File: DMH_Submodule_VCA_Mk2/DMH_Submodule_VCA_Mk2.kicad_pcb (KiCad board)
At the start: 2 copper layers, 41 x 27 mm, 20 parts, among them J1 Conn_01x02, J2 Conn_01x04, Q1 BC548, Q2 BC548, U1 TL072

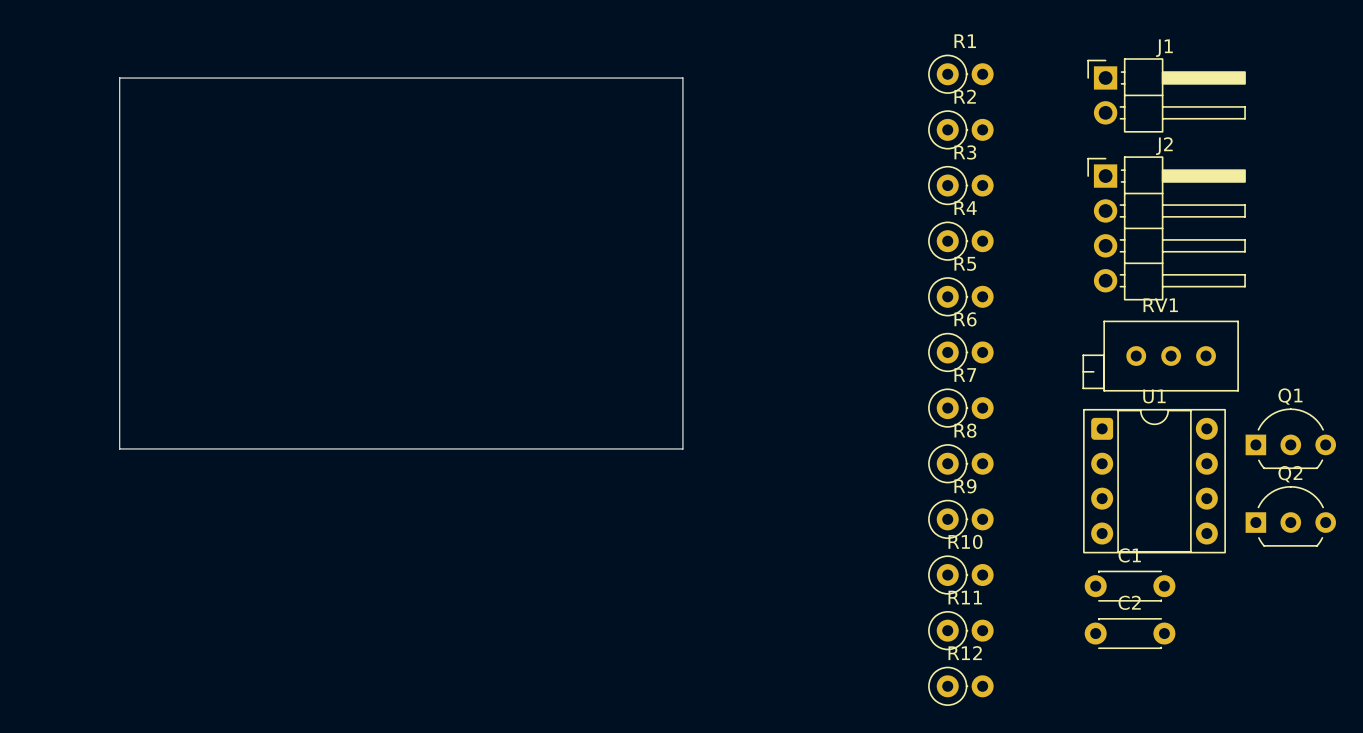
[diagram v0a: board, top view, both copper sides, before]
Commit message: Routed VCA submodule Mk2 PCB
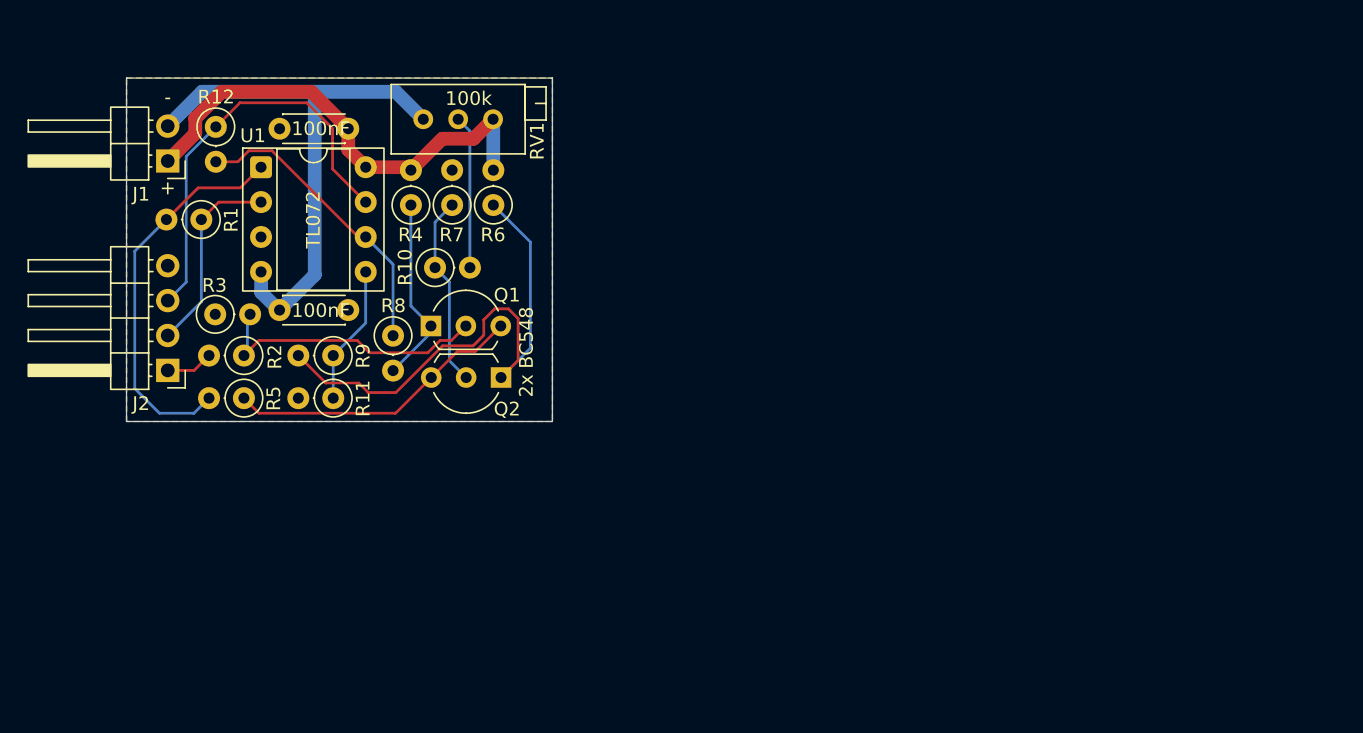
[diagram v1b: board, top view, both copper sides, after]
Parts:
- moved J2 69.7 mm to (57.5, 70.8), turned to 180 degrees
- moved J1 68.5 mm to (57.5, 55.5), turned to 180 degrees
- moved R12 67.1 mm to (61.0, 53.1), turned to -90 degrees
- moved U1 64.1 mm to (64.3, 56.0)
- moved C1 63.8 mm to (70.6, 53.2), turned to 180 degrees
- moved Q1 60.7 mm to (76.7, 67.5)
- moved RV1 59.5 mm to (76.1, 52.5), turned to 180 degrees
- moved C2 59.3 mm to (70.6, 66.4), turned to 180 degrees
- moved Q2 55.9 mm to (81.8, 71.3), turned to 180 degrees
- moved R1 55.3 mm to (59.9, 59.8), turned to 180 degrees
- moved R3 54.1 mm to (61.0, 66.7)
- moved R2 53.8 mm to (63.0, 69.7), turned to 180 degrees
- moved R5 51.8 mm to (63.0, 72.8), turned to 180 degrees
- moved R11 47.8 mm to (69.5, 72.8), turned to 180 degrees
- moved R9 46.3 mm to (69.5, 69.7), turned to 180 degrees
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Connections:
- R10 pad 1: Net-(R10-Pad1) -> Net-(Q2-B)
- R10 pad 2: Net-(Q2-B) -> Net-(R10-Pad2)
- R5 pad 1: Net-(R1-Pad2) -> Net-(Q1-E)
- R5 pad 2: Net-(Q1-E) -> Net-(R1-Pad2)
- R7 pad 1: GND -> Net-(Q2-B)
- R7 pad 2: Net-(Q2-B) -> GND
- RV1 pad 2: Net-(R10-Pad1) -> Net-(R10-Pad2)
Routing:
- net -12V: track 0.00 -> 40.8 mm
- net Net-(Q2-C): track 0.00 -> 40.0 mm
- net +12V: track 0.00 -> 34.9 mm
- net /Signal_Out: track 0.00 -> 30.4 mm
- net Net-(R1-Pad2): track 0.00 -> 28.3 mm
- net Net-(U1B--): track 0.00 -> 21.8 mm
- net Net-(Q1-E): track 0.00 -> 21.8 mm
- net Net-(Q1-B): track 0.00 -> 21.0 mm
- net /CV_Mix_In: track 0.00 -> 14.3 mm
- net Net-(Q2-B): track 0.00 -> 14.0 mm
- net Net-(Q1-C): track 0.00 -> 13.8 mm
- net Net-(R10-Pad2): track 0.00 -> 11.2 mm
- net Net-(U1B-+): track 0.00 -> 10.2 mm
- net /Signal_In: track 0.00 -> 3.45 mm
- added copper zone on B.Cu, net GND
- added copper zone on F.Cu, net GND
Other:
- board size 41 x 27 mm -> 31 x 25 mm
- board text added: "+"
- board text added: "-"
- board text added: "2x"
- board text added: "Mk2.0 July 2026"
- board text removed: "Mk1.0 June 2026"

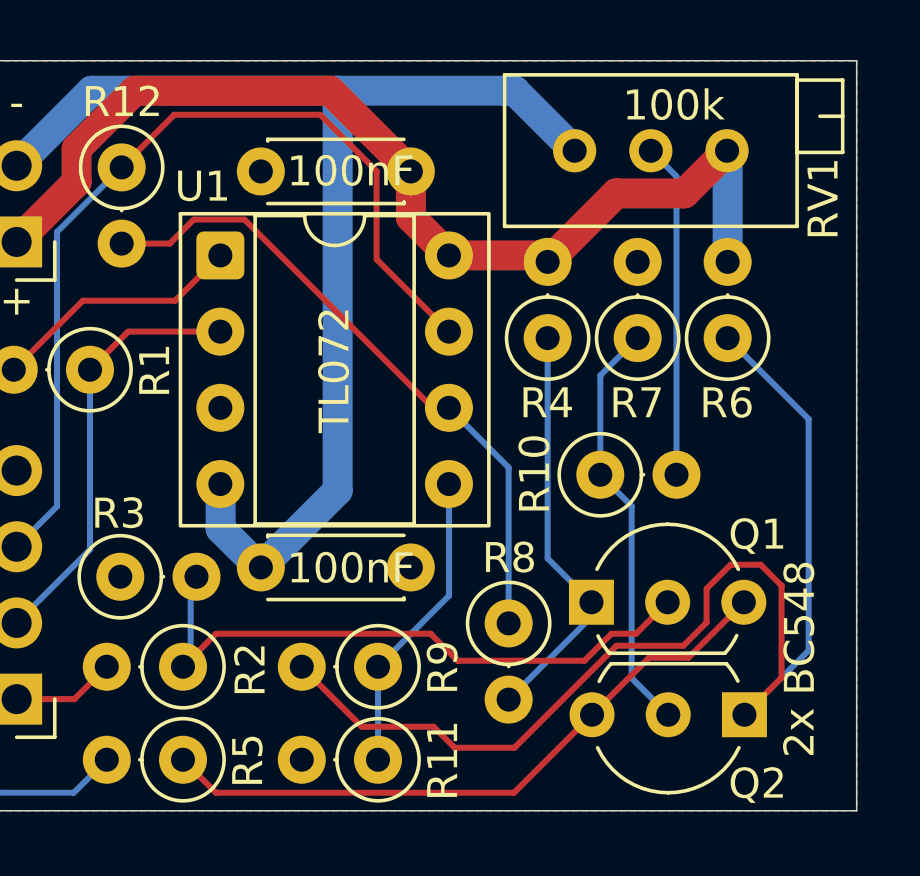
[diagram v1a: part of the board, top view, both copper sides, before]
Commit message: Redesigned PCB
Included solder bridge jumpers to selected between inverting and non-inverting mode. Added C5 for high freq stabilization.
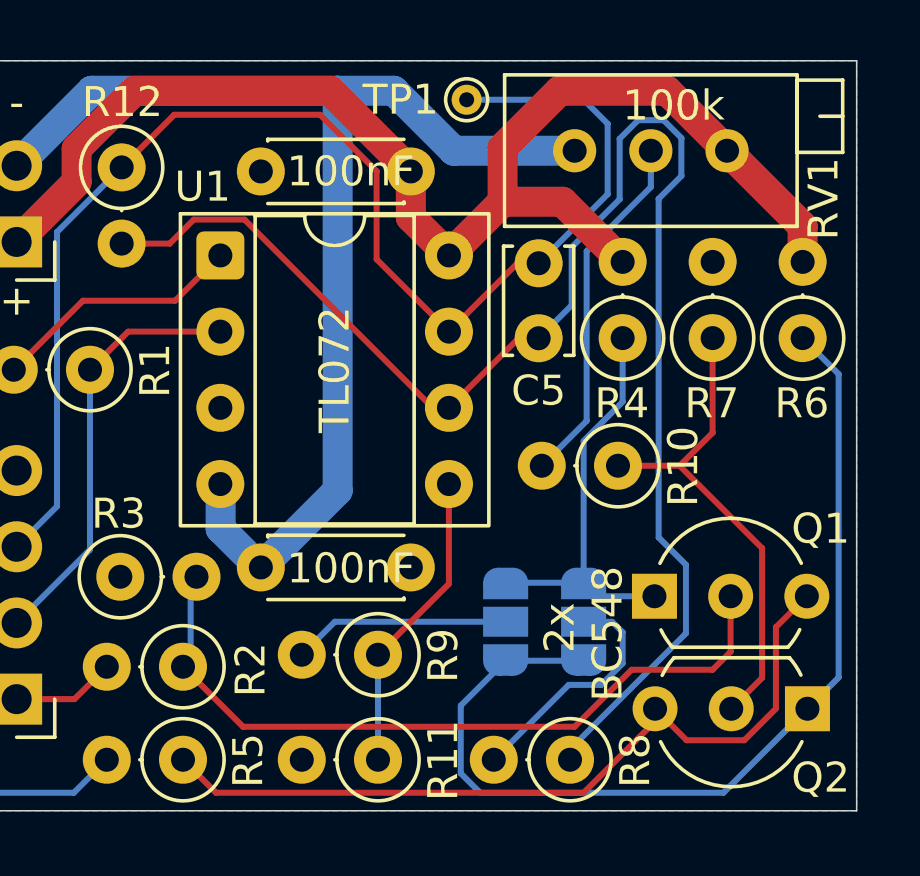
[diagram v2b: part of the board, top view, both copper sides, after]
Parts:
- added C5: 33pF, Capacitor_THT:C_Disc_D3.4mm_W2.1mm_P2.50mm, F.Cu at (74.9, 58.8)
- added JP1: SolderJumper_3_Open, Jumper:SolderJumper-3_P1.3mm_Open_RoundedPad1.0x1.5mm_NumberLabels, B.Cu at (76.4, 68.2)
- added JP2: SolderJumper_3_Open, Jumper:SolderJumper-3_P1.3mm_Open_RoundedPad1.0x1.5mm_NumberLabels, B.Cu at (73.8, 68.2)
- added TP1: TestPoint_Probe, TestPoint:TestPoint_THTPad_D1.0mm_Drill0.5mm, F.Cu at (72.5, 50.8)
- moved R8 4.98 mm to (75.9, 72.8), turned to 180 degrees
- moved R4 2.50 mm to (77.7, 58.7)
- moved R6 2.50 mm to (83.7, 58.7)
- moved R7 2.50 mm to (80.7, 58.7)
- moved Q1 2.11 mm to (78.8, 67.3)
- moved Q2 2.11 mm to (83.9, 71.1)
- moved R10 0.66 mm to (77.5, 63.0), turned to 180 degrees
- moved R9 0.40 mm to (69.5, 69.3)
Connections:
- Q1 pad 1: Net-(Q1-C) -> Net-(JP1-B)
- Q2 pad 1: Net-(Q2-C) -> Net-(JP1-A)
- R4 pad 1: Net-(Q1-C) -> Net-(JP1-B)
- R6 pad 1: Net-(Q2-C) -> Net-(JP1-A)
- R8 pad 2: Net-(Q1-C) -> Net-(JP1-C)
- R9 pad 2: Net-(Q2-C) -> Net-(JP2-C)
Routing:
- net Net-(Q2-C): track 40.0 -> 0.00 mm
- net Net-(JP1-A): track 0.00 -> 33.2 mm
- net Net-(U1B--): track 21.8 -> 51.1 mm
- net /Signal_Out: track 30.4 -> 45.0 mm
- net Net-(JP1-B): track 0.00 -> 13.8 mm
- net Net-(Q1-C): track 13.8 -> 0.00 mm
- net +12V: track 34.9 -> 43.4 mm
- net Net-(JP1-C): track 0.00 -> 8.11 mm
- net Net-(JP2-C): track 0.00 -> 7.25 mm
- net Net-(Q1-E): track 21.8 -> 26.7 mm
- net Net-(Q1-B): track 21.0 -> 25.4 mm
- net Net-(Q2-B): track 14.0 -> 16.4 mm
- net Net-(R10-Pad2): track 11.2 -> 12.0 mm
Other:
- board text added: "1=inv"
- board text added: "3=n.inv"
- board text added: "Mk2.1 October 2026"
- board text removed: "Mk2.0 July 2026"
